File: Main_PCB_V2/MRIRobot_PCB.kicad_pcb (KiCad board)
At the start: 2 copper layers, 172 x 99 mm, 197 parts, among them J1 Conn_01x05, J10 Homing, J11 Homing, J12 Homing, J13 Homing, J14 Homing, J15 Homing, J16 Homing, J17 Conn_01x08, J18 Conn_01x08, J19 Conn_01x08, J2 Conn_01x05, J20 Conn_01x08, J21 Conn_01x08, J22 Conn_01x03, J23 Conn_01x03, J24 Conn_01x08, J25 Conn_01x03, J26 Conn_01x03, J27 Conn_01x08, J3 Conn_01x05, J4 USB_C_Receptacle_USB2.0_16P, J5 Conn_01x05, J6 Conn_01x05, J7 Conn_01x05, J8 Conn_01x05, J9 Power In, SW1 5V Enable, SW2 3.3V Enable, SW3 Toggle_Switch0, SW4 Toggle_Switch1, SW5 Toggle_Switch2, SW6 Toggle_Switch3, U1 NUCLEO-F446RE, U2 FT231XS, U3 CMOD_A7_FPGA, U4 LM22676MR-5, U5 LM22676MR-ADJ

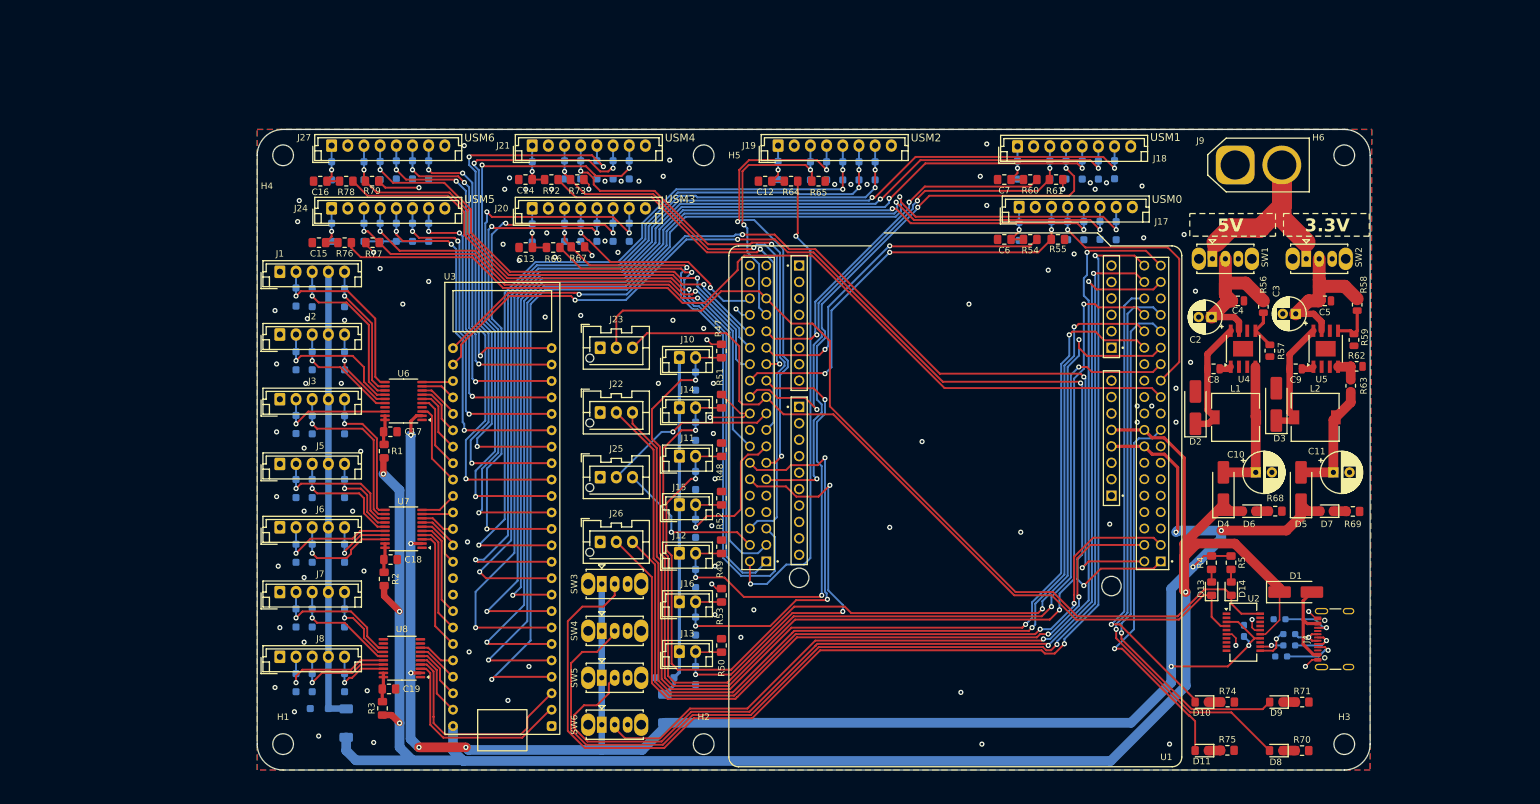
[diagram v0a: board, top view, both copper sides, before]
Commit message: finished new PCB and ordered
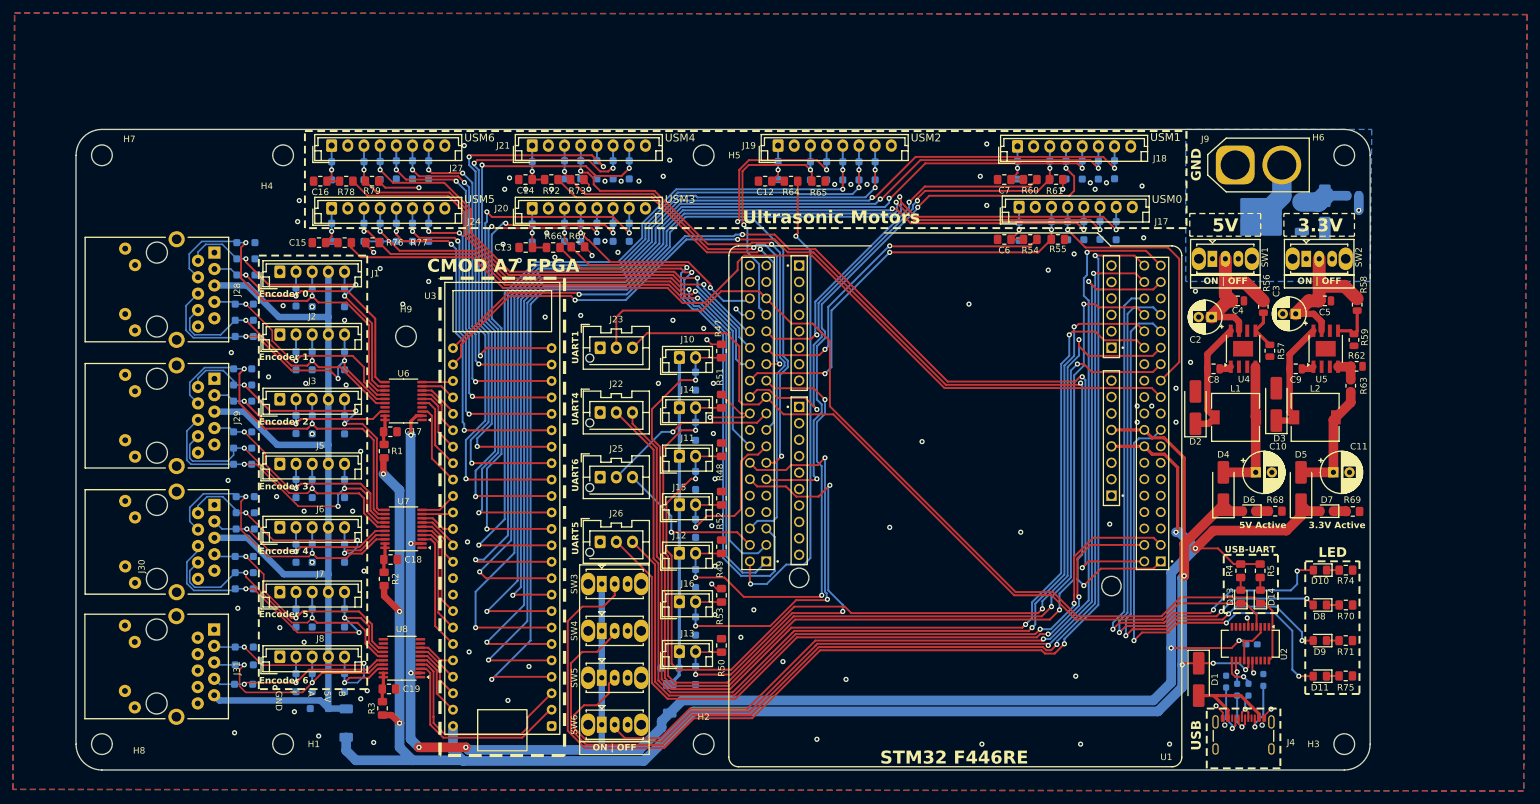
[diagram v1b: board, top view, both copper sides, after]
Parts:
- added D100: D_TVS, Diode_SMD:D_SOD-123F, B.Cu at (52.1, 127.2)
- added D101: D_TVS, Diode_SMD:D_SOD-123F, B.Cu at (52.0, 139.0)
- added D102: D_TVS, Diode_SMD:D_SOD-123F, B.Cu at (52.1, 124.8)
- added D103: D_TVS, Diode_SMD:D_SOD-123F, B.Cu at (52.0, 136.5)
- added D104: D_TVS, Diode_SMD:D_SOD-123F, B.Cu at (52.1, 129.8)
- added D105: D_TVS, Diode_SMD:D_SOD-123F, B.Cu at (52.0, 134.0)
- added D106: D_TVS, Diode_SMD:D_SOD-123F, B.Cu at (52.0, 148.0)
- added D107: D_TVS, Diode_SMD:D_SOD-123F, B.Cu at (52.0, 150.8)
- added D108: D_TVS, Diode_SMD:D_SOD-123F, B.Cu at (51.9, 153.8)
- added D109: D, Diode_SMD:D_SMA_Handsoldering, B.Cu at (219.0, 80.8)
- added D88: D_TVS, Diode_SMD:D_SOD-123F, B.Cu at (52.2, 88.0)
- added D89: D_TVS, Diode_SMD:D_SOD-123F, B.Cu at (52.0, 100.0)
- added D90: D_TVS, Diode_SMD:D_SOD-123F, B.Cu at (52.2, 85.5)
- added D91: D_TVS, Diode_SMD:D_SOD-123F, B.Cu at (52.0, 97.5)
- added D92: D_TVS, Diode_SMD:D_SOD-123F, B.Cu at (52.2, 90.5)
- added D93: D_TVS, Diode_SMD:D_SOD-123F, B.Cu at (52.0, 95.0)
- added D94: D_TVS, Diode_SMD:D_SOD-123F, B.Cu at (51.8, 107.5)
- added D95: D_TVS, Diode_SMD:D_SOD-123F, B.Cu at (51.8, 119.8)
- added D96: D_TVS, Diode_SMD:D_SOD-123F, B.Cu at (51.8, 105.0)
- added D97: D_TVS, Diode_SMD:D_SOD-123F, B.Cu at (51.8, 117.2)
- added D98: D_TVS, Diode_SMD:D_SOD-123F, B.Cu at (51.8, 110.0)
- added D99: D_TVS, Diode_SMD:D_SOD-123F, B.Cu at (51.8, 114.8)
- added H7: MountingHole, MountingHole:MountingHole_3.2mm_M3, F.Cu at (30.0, 72.0)
- added H8: MountingHole, MountingHole:MountingHole_3.2mm_M3, F.Cu at (30.0, 163.0)
- added H9: MountingHole, MountingHole:MountingHole_3.2mm_M3, F.Cu at (77.0, 100.0)
- added J28: RJ45_RB1-125B8G1A, Connector_RJ:RJ45_UDE_RB1-125B8G1A, F.Cu at (47.4, 87.0)
- added J29: RJ45_RB1-125B8G1A, Connector_RJ:RJ45_UDE_RB1-125B8G1A, F.Cu at (47.4, 106.5)
- added J30: RJ45_RB1-125B8G1A, Connector_RJ:RJ45_UDE_RB1-125B8G1A, F.Cu at (47.4, 126.0)
- added J31: RJ45_RB1-125B8G1A, Connector_RJ:RJ45_UDE_RB1-125B8G1A, F.Cu at (47.4, 145.3)
- added Q1: SUD08P06-155L, Package_TO_SOT_SMD:TO-252-2, B.Cu at (210.4, 81.5)
- added R6: 100K, Resistor_SMD:R_0805_2012Metric, B.Cu at (223.3, 78.2)
- U6, U7, U8: value ~ -> LSF0108
- moved D10 27.4 mm to (218.2, 136.1)
- moved R74 27.4 mm to (222.2, 136.1)
- moved R70 23.5 mm to (222.2, 141.5)
- moved D8 23.5 mm to (218.2, 141.5)
- moved J4 22.0 mm to (206.4, 162.7), turned to 0 degrees
- moved R75 21.6 mm to (222.2, 152.5)
- moved D11 21.6 mm to (218.2, 152.5)
- moved D1 20.2 mm to (199.5, 153.0), turned to -90 degrees
- moved D9 11.6 mm to (218.2, 147.0)
- moved R71 11.6 mm to (222.2, 147.0)
- moved R22 10.7 mm to (207.2, 154.6), turned to 90 degrees
- moved R21 10.6 mm to (205.4, 154.6), turned to 90 degrees
- moved R13 9.71 mm to (209.5, 153.1), turned to 90 degrees
- moved R14 9.35 mm to (203.7, 153.3), turned to 90 degrees
- moved D14 4.68 mm to (209.0, 140.2)
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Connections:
- J9 pad 2: +24V -> Net-(J9-Pin_2)
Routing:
- net /5V_E: track 70.3 -> 148.1 mm
- net /B5: track 13.0 -> 53.4 mm, vias 1 -> 3
- net +24V: track 37.6 -> 0.00 mm
- net /B3: track 13.8 -> 50.2 mm, vias 1 -> 3
- net /B1: track 13.3 -> 49.7 mm, vias 1 -> 3
- net /B4: track 11.6 -> 44.2 mm, vias 1 -> 3
- net /A0: track 26.2 -> 58.6 mm, vias 1 -> 2
- net /A2: track 27.1 -> 59.1 mm, vias 1 -> 2
- net /B2: track 21.9 -> 53.8 mm, vias 1 -> 3
- net /A4: track 17.1 -> 48.8 mm, vias 1 -> 2
- net /B0: track 20.9 -> 52.5 mm, vias 1 -> 3
- net /B6: track 10.9 -> 40.8 mm, vias 1 -> 3
- net /A5: track 17.4 -> 46.3 mm, vias 1 -> 2
- net /A3: track 18.9 -> 46.5 mm, vias 1 -> 2
- net /A1: track 18.0 -> 45.0 mm, vias 1 -> 2
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- added copper zone on B.Cu, net +24V
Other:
- board size 172 x 99 mm -> 200 x 99 mm
- board text added: "3.3V Active"
- board text added: "5V Active"
- board text added: "A"
- board text added: "B"
- board text added: "CMOD A7 FPGA"
- board text added: "Encoder 0"
- board text added: "Encoder 1"
- board text added: "Encoder 2"
- board text added: "Encoder 3"
- board text added: "Encoder 4"
- board text added: "Encoder 5"
- board text added: "Encoder 6"
- board text added: "I"
- board text added: "LED"
- board text added: "ON | OFF"
- board text added: "STM32 F446RE"
- board text added: "UART1"
- board text added: "UART4"
- board text added: "UART5"
- board text added: "UART6"
- board text added: "USB"
- board text added: "USB-UART"
- board text added: "Ultrasonic Motors"
